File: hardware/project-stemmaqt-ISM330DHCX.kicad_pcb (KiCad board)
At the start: 4 copper layers, 25.4 x 17.8 mm, 20 parts, among them J1 SM04B-SRSS-TB(LF)(SN), J2 SM04B-SRSS-TB(LF)(SN), J3 SM04B-SRSS-TB(LF)(SN), U1 TPS7A0218PDBVR, U2 AS7341-DLGT

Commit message: First draft
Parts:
- removed R4: PU, Resistor_SMD:R_0603_1608Metric
- removed U2: AS7341-DLGT, AS7341-DLGT:PSON80P310X200X110-8N
- added ?: , , F.Cu at (53.0, 58.0)
- added ?: , , F.Cu at (46.9, 58.0)
- C1: value 1uF -> 10uF
- C2: value 1uF -> 0.1uF; footprint Capacitor_SMD:C_0805_2012Metric -> Capacitor_SMD:C_0603_1608Metric
- J3: value SM04B-SRSS-TB(LF)(SN) -> Conn_01x04_Male; footprint SM04B-SRSS-TB(LF)(SN):JST_SM04B-SRSS-TB(LF)(SN) -> Connector_PinHeader_2.54mm:PinHeader_1x04_P2.54mm_Vertical
- U1: value TPS7A0218PDBVR -> ISM330DHCXTR; footprint TPS7A0233PDBVR:SOT95P280X145-5N -> ISM330DHCXTR:PQFN50P250X300X86-14N
- moved C1 13.8 mm to (52.7, 66.7), turned to 180 degrees
- moved JP1 13.0 mm to (42.3, 57.3), turned to 270 degrees
- moved C2 8.70 mm to (48.9, 65.9), turned to 0 degrees
- moved U1 6.84 mm to (48.9, 63.6)
- moved J3 4.30 mm to (43.3, 71.0), turned to 90 degrees
- moved R1 2.97 mm to (44.3, 67.2)
- moved R2 2.97 mm to (44.3, 65.7)
- moved C3 2.29 mm to (51.4, 63.6)
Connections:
- C2 pad 1: +1V8 -> VCC
- C3 pad 1: +1V8 -> VCC
- J3 pad 1: /EN -> GND
- J3 pad 2: /GPIO -> VCC
- J3 pad 3: /INT -> /INT1
- J3 pad 4: GND -> /INT2
- JP1 pad 1: /EN -> GND
- JP1 pad 2: Net-(JP1-Pad2) -> /SA0
- R1 pad 2: /INT -> /SCL
- R2 pad 2: /SCL -> /SDA
- U1 pad 1: VCC -> /SA0
- U1 pad 3: Net-(JP1-Pad2) -> GND
- U1 pad 4: (no net) -> /INT1
- U1 pad 5: +1V8 -> VCC
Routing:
- net /EN: track 22.5 -> 0.00 mm, vias 2 -> 0
- net /GPIO: track 18.9 -> 0.00 mm, vias 2 -> 0
- net /INT: track 13.5 -> 0.00 mm, vias 3 -> 0
- net /INT2: track 0.00 -> 10.7 mm
- net Net-(JP1-Pad2): track 10.5 -> 0.00 mm, vias 2 -> 0
- net /SA0: track 0.00 -> 9.85 mm, vias 0 -> 2
- net +1V8: track 9.75 -> 0.00 mm, vias 2 -> 0
- net /INT1: track 0.00 -> 7.21 mm
- net VCC: track 8.15 -> 12.7 mm, vias 8 -> 10
- net /SCL: track 24.2 -> 27.8 mm
- net /SDA: track 23.9 -> 20.3 mm, vias 0 -> 2
- net GND: track 16.4 -> 19.4 mm, vias 15 -> 13
- removed copper zone on F.Cu, net +1V8
- removed copper zone on F.Cu, net GND
- removed copper zone on F.Cu, net VCC
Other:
- rule trace_min: 0.2 -> 0.127
- rule via_min_drill: 0.3 -> 0.254
- board text added: "1"
- board text added: "2"
- board text added: "GND"
- board text added: "StemmaQT ISM330DHCX"
- board text added: "V+"
- board text removed: "Stemma AS7341"

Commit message: Add the battery and interrupt graphics
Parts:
- removed U$30, U$31: , stemmaqt_shift:STEMMAQT
- added Ref**: Val**, hardware:ISM330DHCX Stemma interrupts, F.Cu at (51.6, 68.2)
- added Ref**: Val**, hardware:Batería, F.Cu at (43.9, 69.3)
- added Ref**: Val**, hardware:Firma François, B.Cu at (51.7, 52.6)
- turned C1 to 0 degrees
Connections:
- J3 pad 1: GND -> VCC
- J3 pad 2: VCC -> GND
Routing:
- net GND: track 19.4 -> 22.0 mm, vias 13 -> 12
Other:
- board text added: "Francois Gervais"
- board text added: "INT"
- board text removed: "StemmaQT ISM330DHCX"

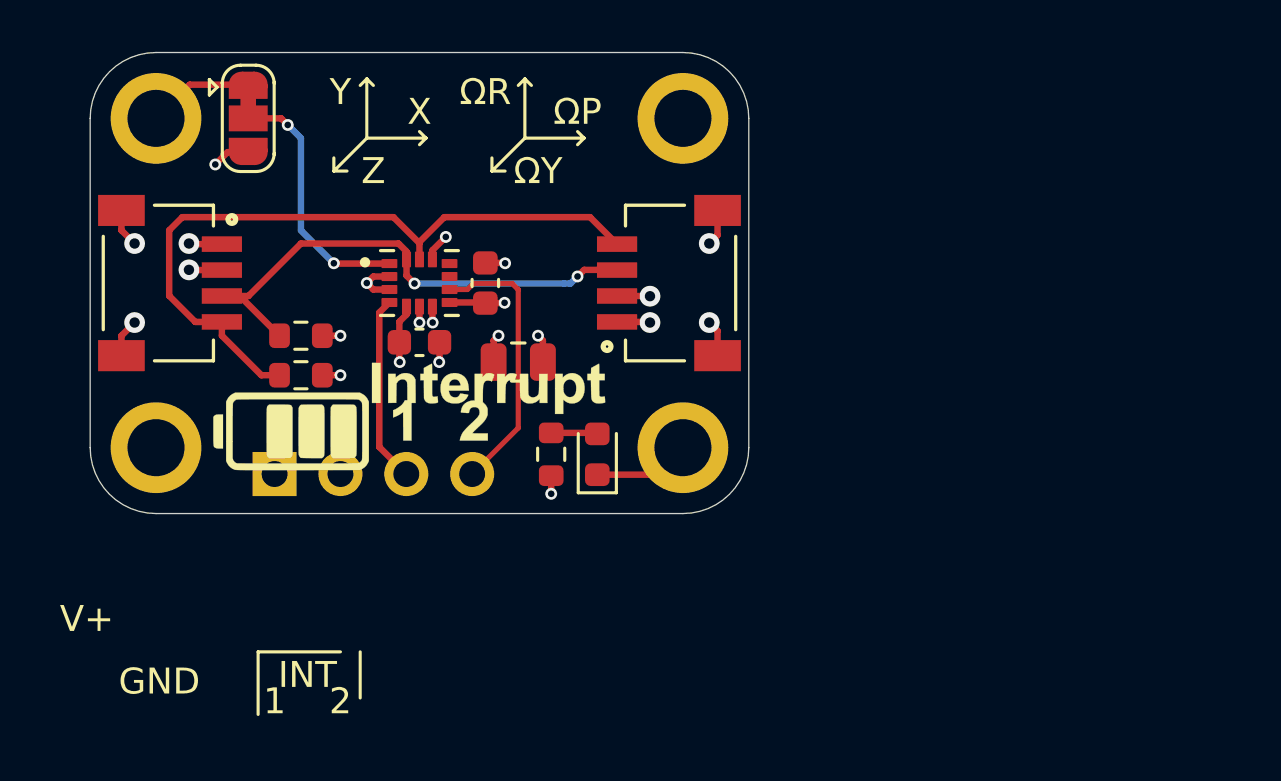
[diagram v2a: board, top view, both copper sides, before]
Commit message: Add the board title graphic
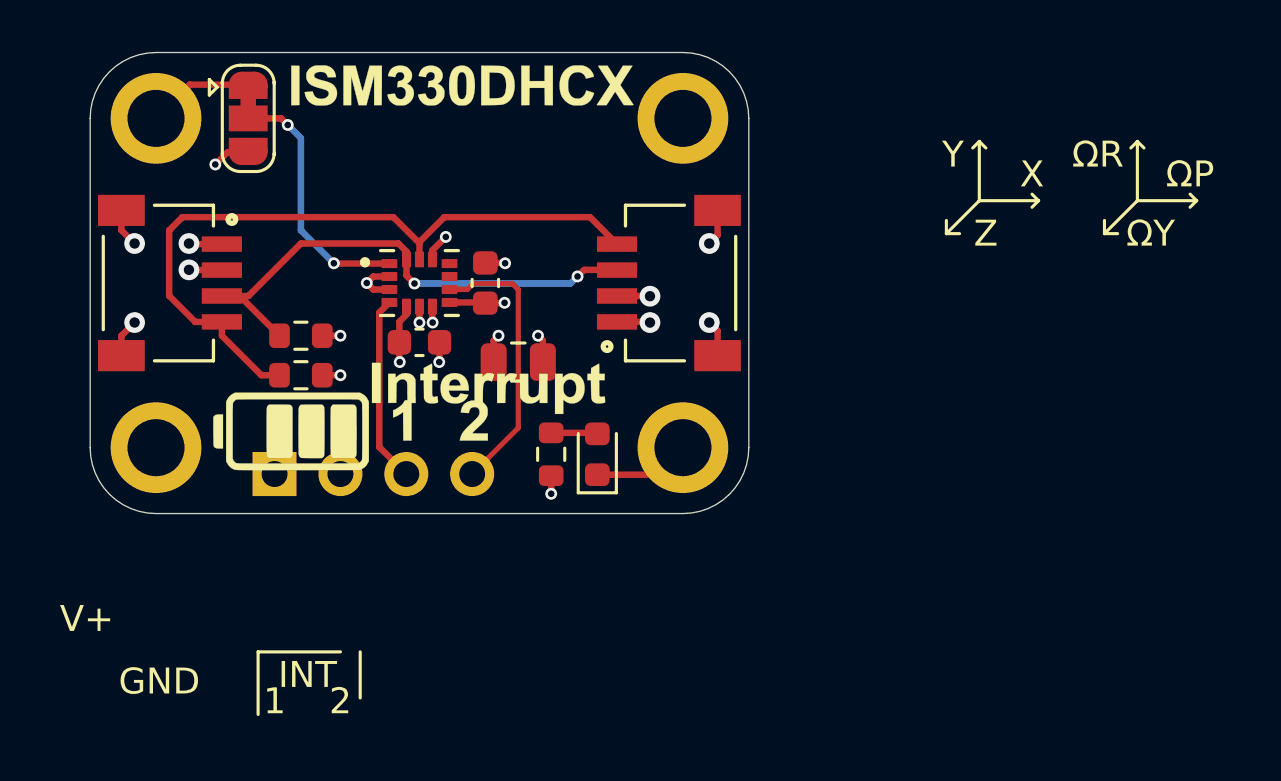
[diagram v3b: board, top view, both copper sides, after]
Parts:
- added Ref**: Val**, hardware:ISM330DHCX, F.Cu at (50.5, 56.0)
- moved ? 23.7 mm to (76.6, 60.5)
- moved ? 23.7 mm to (70.5, 60.5)

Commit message: Add the bunny logo
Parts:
- added Ref**: Val**, hardware:bunny-01, B.Cu at (53.7, 63.1)
- moved Ref** 2.29 mm to (49.4, 52.7)

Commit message: Add graphics
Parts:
- removed the Ref** at (49.4, 52.7)
- moved ? 23.9 mm to (52.7, 59.9)
- moved ? 23.9 mm to (46.6, 59.9)
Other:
- board text removed: "1"
- board text removed: "2"
- board text removed: "GND"
- board text removed: "INT"
- board text removed: "V+"

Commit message: Write my name correctly
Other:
- board text added: "François Gervais"
- board text removed: "Francois Gervais"
